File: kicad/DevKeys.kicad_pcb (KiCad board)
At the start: 2 copper layers, 12 parts, among them J1 RaspberryPiZeroW, J2 Display

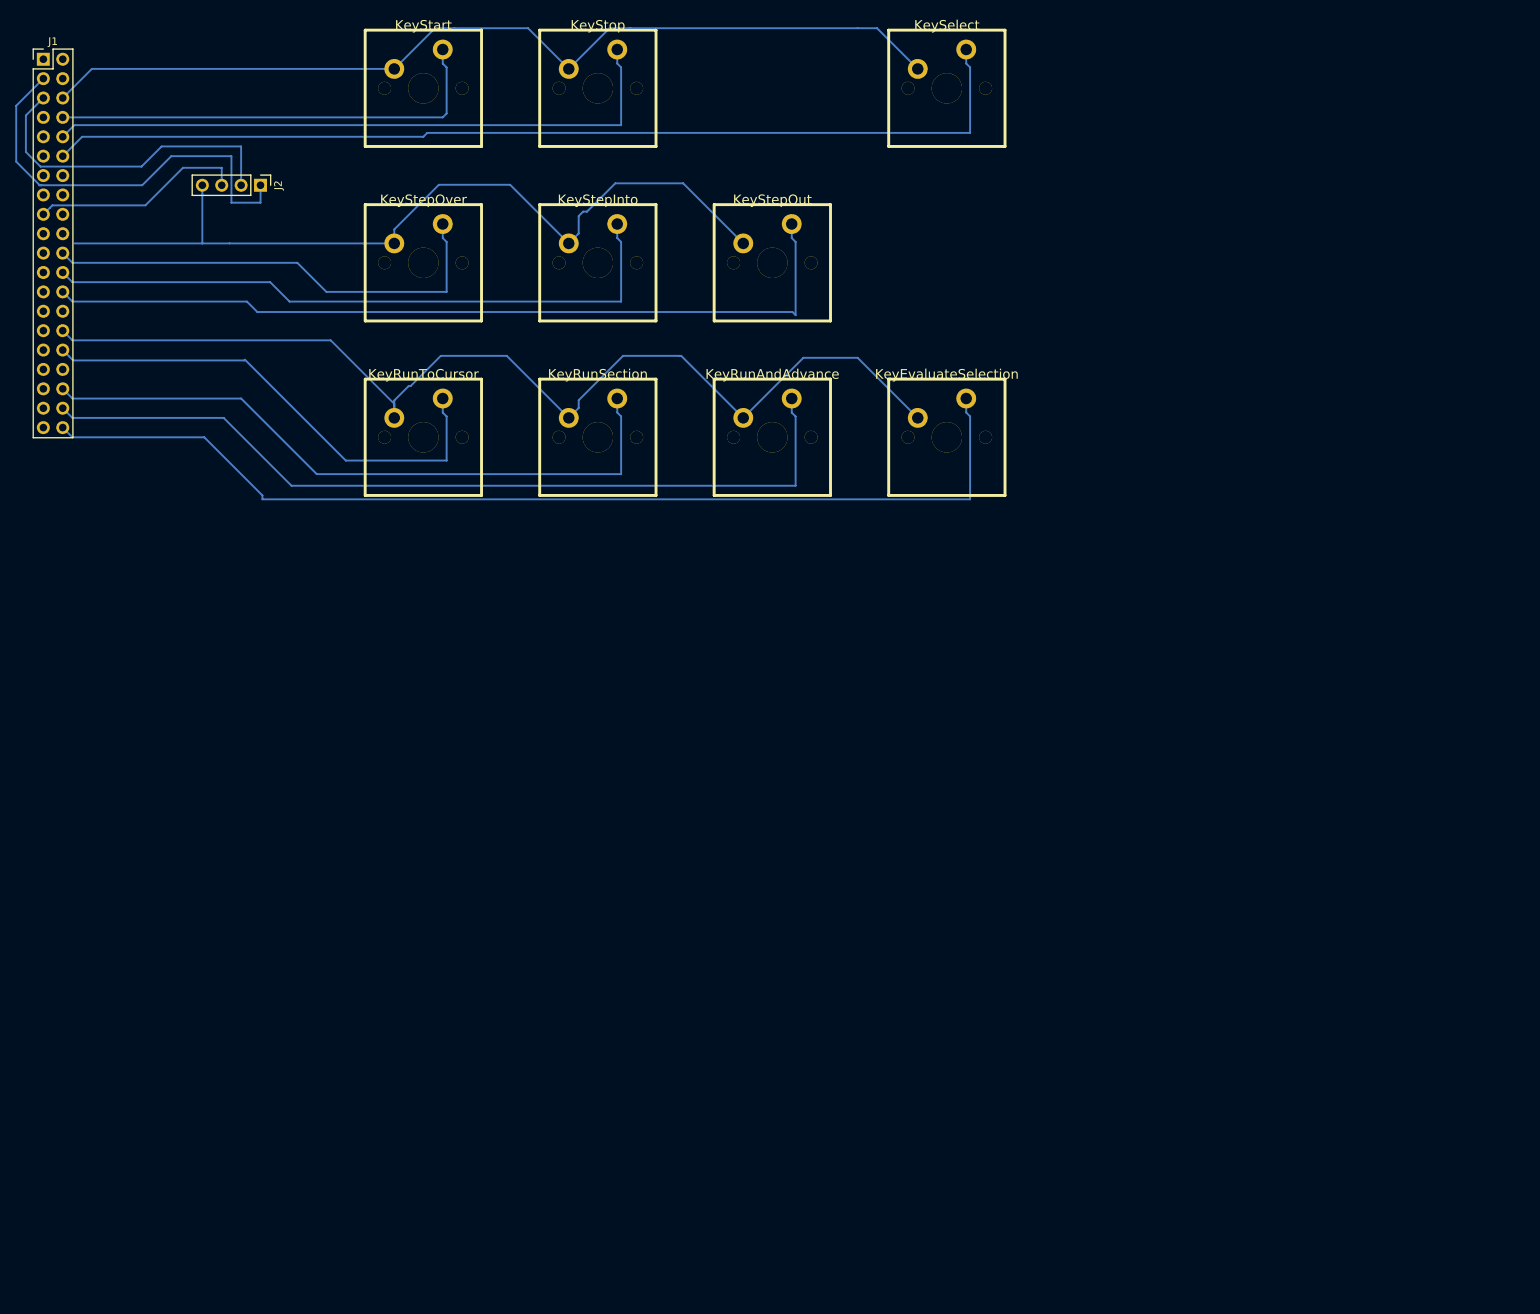
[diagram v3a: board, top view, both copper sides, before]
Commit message: Layout angepasst zum ätzen.
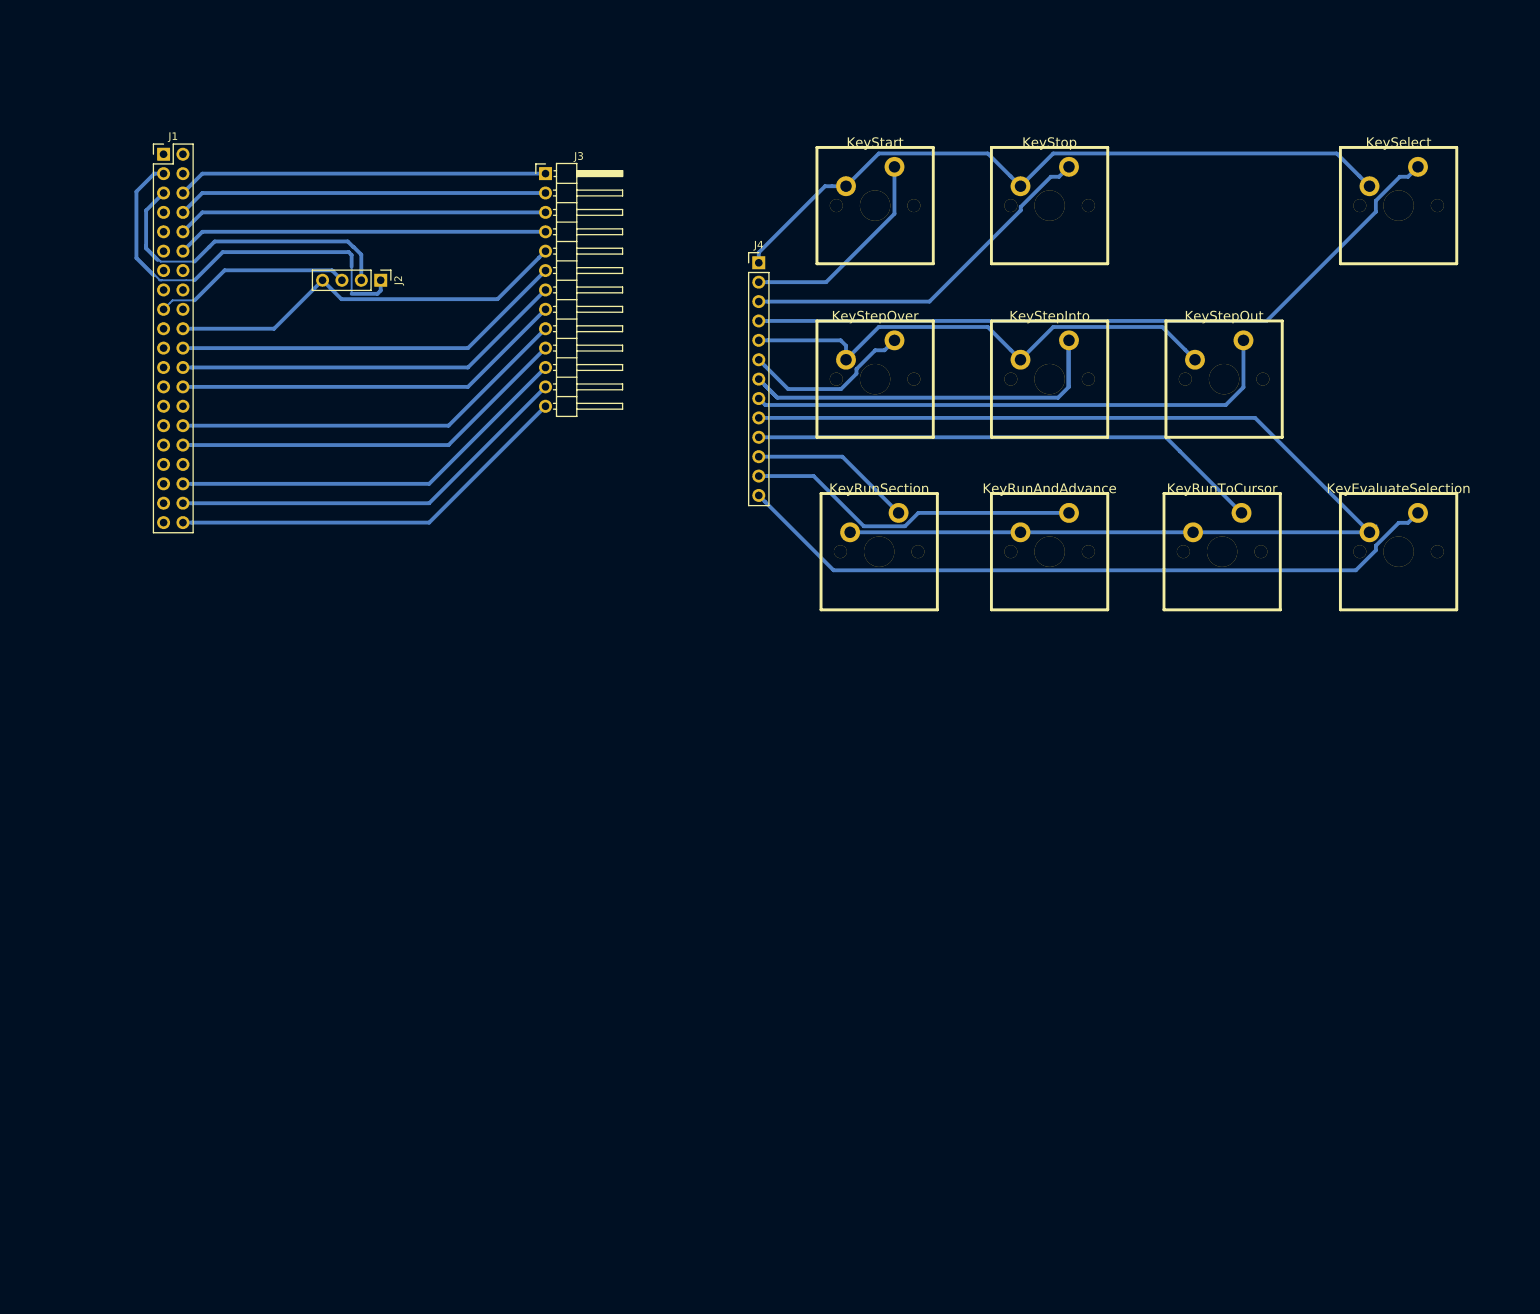
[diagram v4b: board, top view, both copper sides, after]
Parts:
- added J3: Conn_01x13_Male, Pin_Headers:Pin_Header_Angled_1x13_Pitch2.54mm, F.Cu at (71.6, 20.8)
- added J4: Conn_01x13_Female, Pin_Headers:Pin_Header_Straight_1x13_Pitch2.54mm, F.Cu at (99.6, 32.5)
- S2: value KeyStop -> KeyStepOver
- S3: value KeySelect -> KeyRunToCursor
- S4: value KeyStepOver -> KeyStop
- S6: value KeyStepOut -> KeyRunSection
- S7: value KeyRunToCursor -> KeyStepOut
- S8: value KeyRunSection -> KeyRunAndAdvance
- S9: value KeyRunAndAdvance -> KeySelect
- moved S7 105.2 mm to (160.5, 47.8)
- moved S9 87.5 mm to (183.4, 25.0)
- moved S4 82.4 mm to (137.7, 25.0)
- moved S3 70.6 mm to (160.3, 70.4)
- moved S1 61.1 mm to (114.8, 25.0)
- moved S5 61.1 mm to (137.7, 47.8)
- moved S10 61.0 mm to (183.4, 70.4)
- moved S8 61.0 mm to (137.7, 70.4)
- moved S2 52.6 mm to (114.8, 47.8)
- moved S6 40.4 mm to (115.3, 70.4)
- moved J1 20.1 mm to (21.6, 18.3)
- moved J2 20.1 mm to (50.0, 34.8)
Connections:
- S1 pad 1: Net-(J1-Pad6) -> Net-(J4-Pad1)
- S1 pad 2: Net-(J1-Pad8) -> Net-(J4-Pad2)
- S10 pad 1: Net-(J1-Pad30) -> Net-(J4-Pad9)
- S10 pad 2: Net-(J1-Pad40) -> Net-(J4-Pad13)
- S2 pad 1: Net-(J1-Pad6) -> Net-(J4-Pad5)
- S2 pad 2: Net-(J1-Pad10) -> Net-(J4-Pad6)
- S3 pad 1: Net-(J1-Pad6) -> Net-(J4-Pad9)
- S3 pad 2: Net-(J1-Pad12) -> Net-(J4-Pad10)
- S4 pad 1: Net-(J1-Pad20) -> Net-(J4-Pad1)
- S4 pad 2: Net-(J1-Pad22) -> Net-(J4-Pad3)
- S5 pad 1: Net-(J1-Pad20) -> Net-(J4-Pad5)
- S5 pad 2: Net-(J1-Pad24) -> Net-(J4-Pad7)
- S6 pad 1: Net-(J1-Pad20) -> Net-(J4-Pad9)
- S6 pad 2: Net-(J1-Pad26) -> Net-(J4-Pad11)
- S7 pad 1: Net-(J1-Pad30) -> Net-(J4-Pad5)
- S7 pad 2: Net-(J1-Pad32) -> Net-(J4-Pad8)
- S8 pad 1: Net-(J1-Pad30) -> Net-(J4-Pad9)
- S8 pad 2: Net-(J1-Pad36) -> Net-(J4-Pad12)
- S9 pad 1: Net-(J1-Pad30) -> Net-(J4-Pad1)
- S9 pad 2: Net-(J1-Pad38) -> Net-(J4-Pad4)
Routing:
- net Net-(J4-Pad9): track 0.00 -> 178.9 mm
- net Net-(J4-Pad4): track 0.00 -> 95.6 mm
- net Net-(J4-Pad7): track 0.00 -> 95.3 mm
- net Net-(J4-Pad13): track 0.00 -> 93.9 mm
- net Net-(J4-Pad1): track 0.00 -> 92.1 mm
- net Net-(J1-Pad30): track 139.7 -> 52.8 mm
- net Net-(J1-Pad12): track 131.3 -> 48.6 mm
- net Net-(J1-Pad40): track 136.5 -> 53.8 mm
- net Net-(J1-Pad6): track 122.7 -> 48.6 mm
- net Net-(J4-Pad8): track 0.00 -> 71.0 mm
- net Net-(J4-Pad10): track 0.00 -> 67.3 mm
- net Net-(J4-Pad5): track 0.00 -> 66.4 mm
- net Net-(J1-Pad38): track 111.9 -> 53.8 mm
- net Net-(J1-Pad26): track 109.4 -> 51.7 mm
- net Net-(J1-Pad20): track 110.6 -> 53.8 mm
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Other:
- net class Default: trace_width 0.25 -> 0.5
- net class Verjüngt added: clearance 0.2, trace_width 0.25, via_dia 0.6, via_drill 0.4
